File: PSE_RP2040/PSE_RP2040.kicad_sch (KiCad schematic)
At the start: 68 parts, among them IC2 SAM-M8Q-0, J1 USB_B, J2 USB_B_Mini, J3 8P8C_LED, J4 Conn_01x03, Q2 IRLML6402, SW1 SW_Push, SW2 SW_Push, U1 RP2040, U2 PCF8563T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

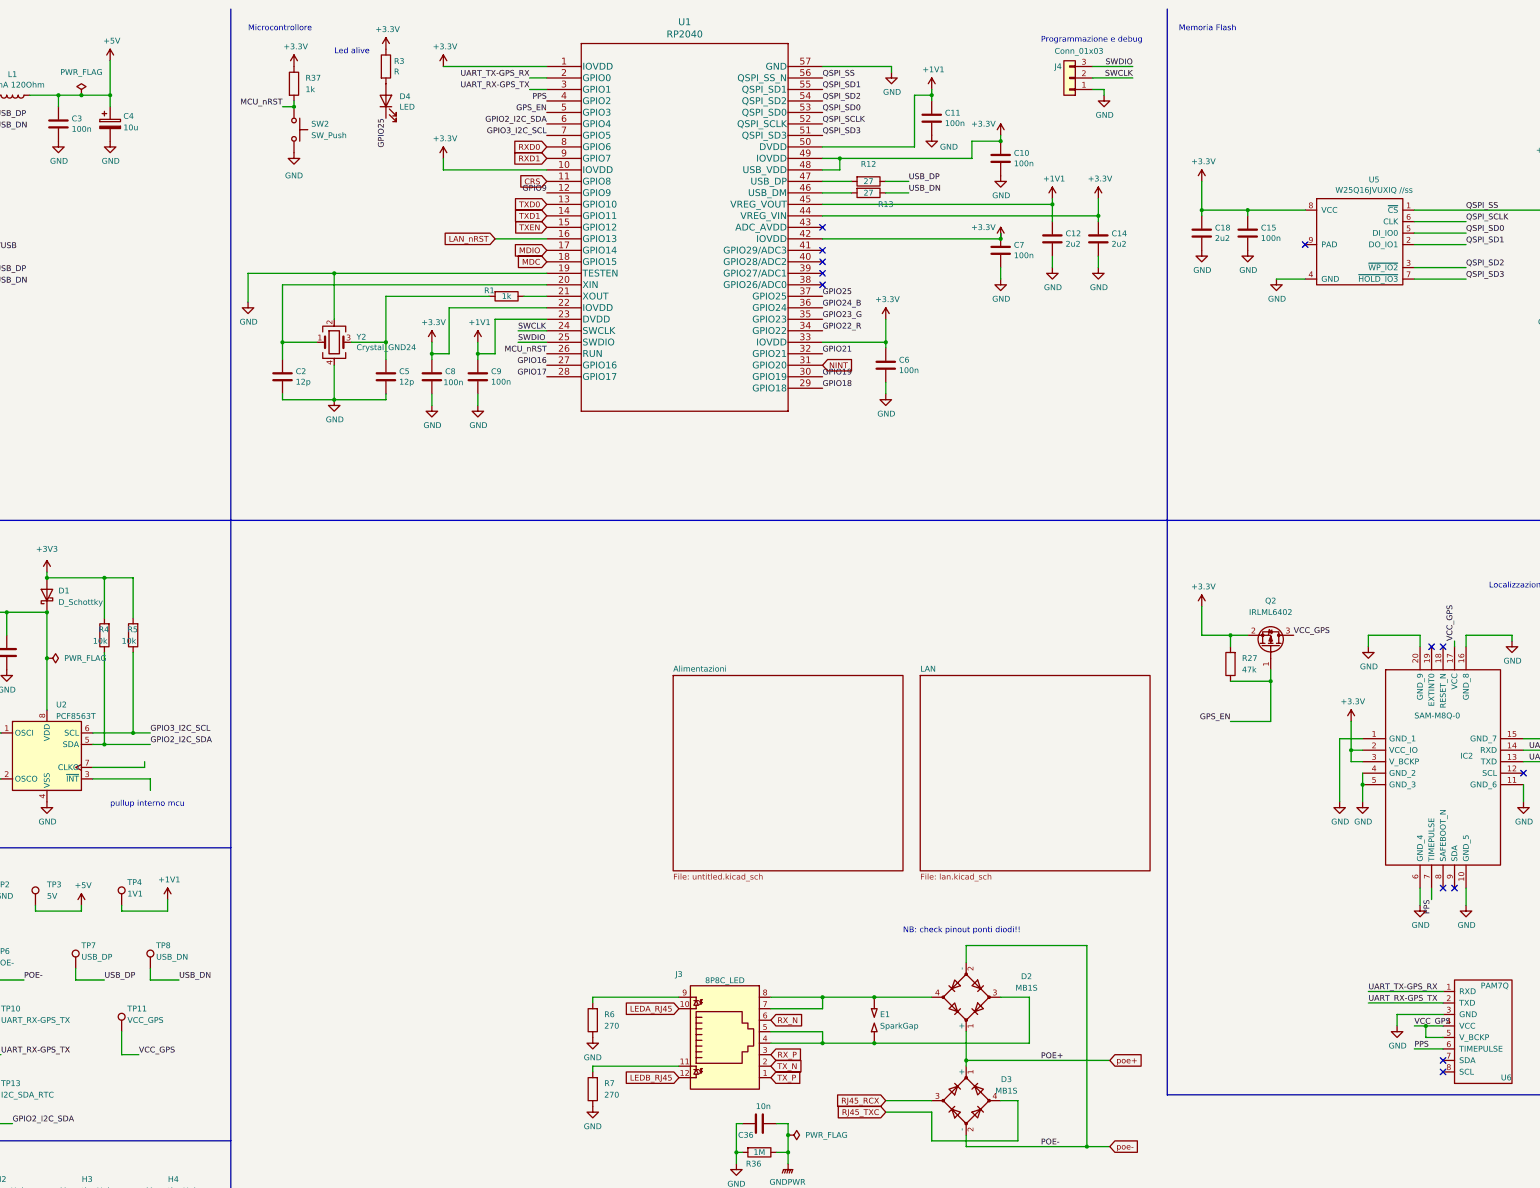
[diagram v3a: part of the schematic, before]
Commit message: check pin, footprint e symb mem
tolto pin 9 al simbolo memoria
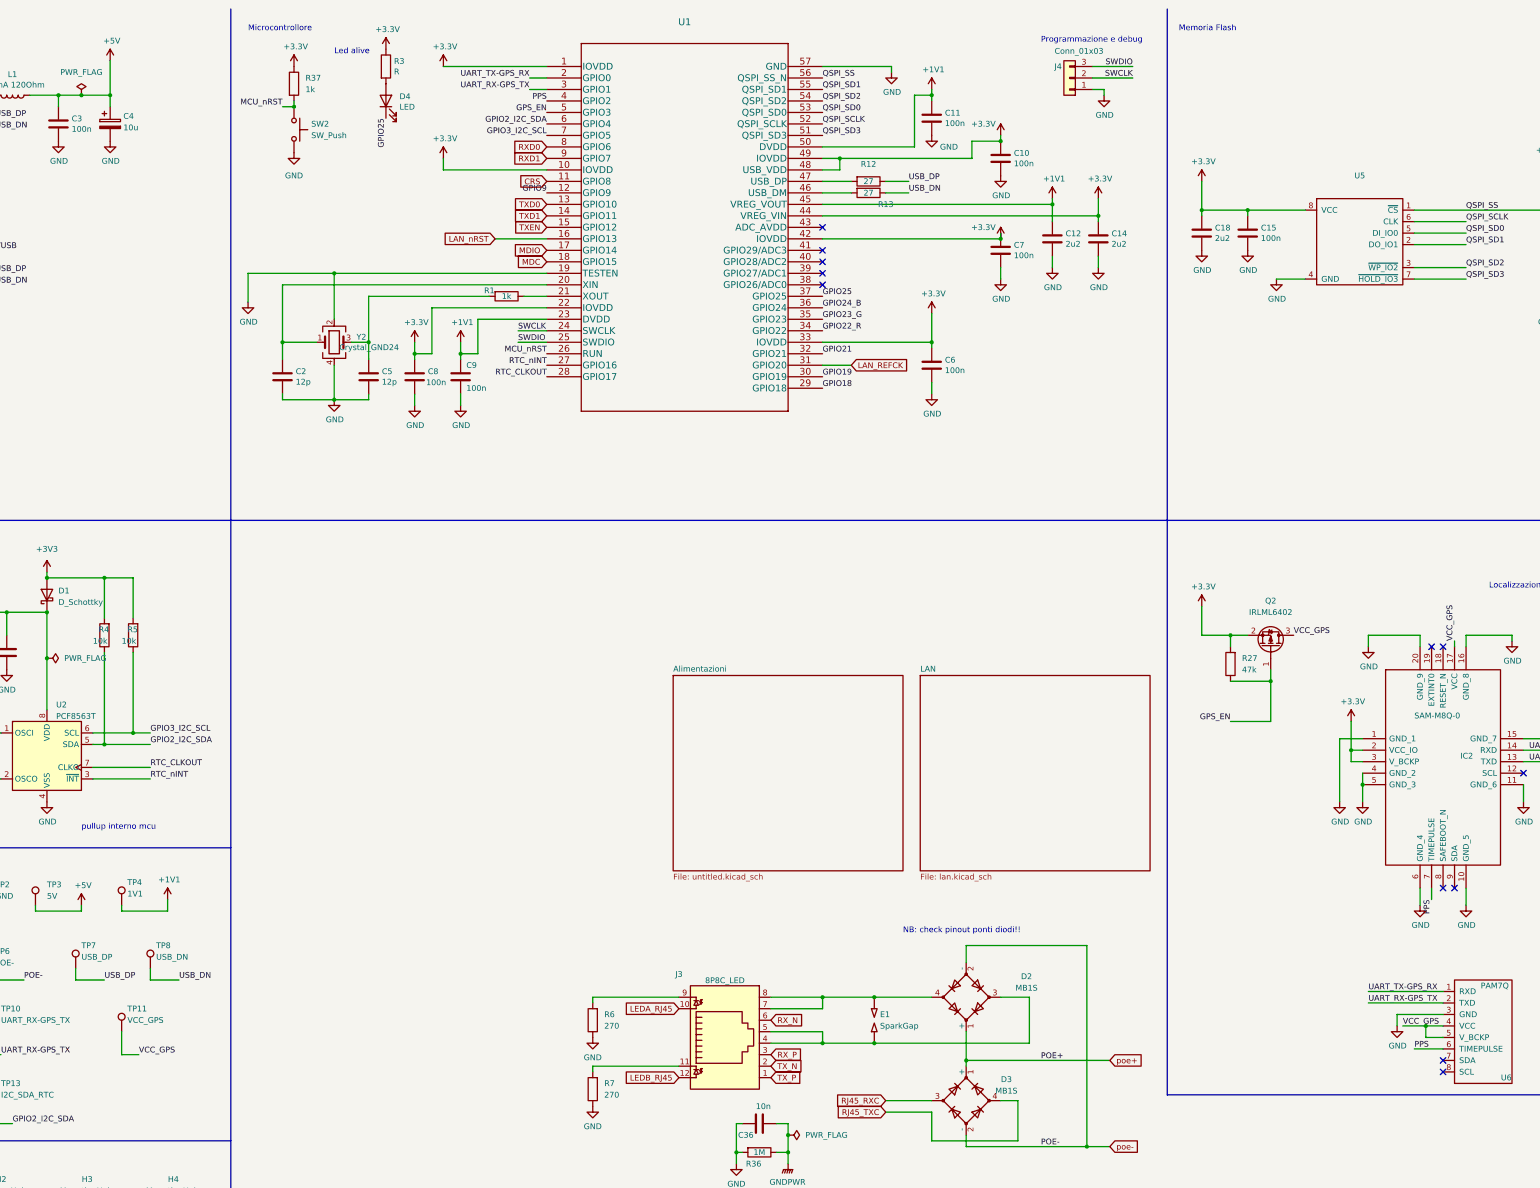
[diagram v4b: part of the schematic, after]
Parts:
- removed U5: W25Q16JVUXIQ //ss, Package_SO:SOIC-8_5.275x5.275mm_P1.27mm, symbol PSE_RP2040-rescue:W25Q16JVUXIQ-Flash_memory
- added U5: (no value), symbol pse_paganin:W25Q16JVUXIQ
- U1: value RP2040 -> (none); footprint PSE2021:RP2040-QFN-56 -> (none)
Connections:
- net GPIO16 is gone; now on net RTC_nINT: U1.27 (GPIO16)
- net GPIO17 is gone; now on net RTC_CLKOUT: U1.28 (GPIO17)
- net +3V3: now also U5.8 (VCC)
- net GND: now also U5.4 (GND)
- net QSPI_SCLK: now also U5.6 (CLK)
- net QSPI_SD0: now also U5.5 (DI_IO0)
- net QSPI_SD1: now also U5.2 (DO_IO1)
- net QSPI_SD2: now also U5.3 (~{WP_IO2})
- net QSPI_SD3: now also U5.7 (~{HOLD_IO3})
- net QSPI_SS: now also U5.1 (~{CS})
- net RTC_nINT: now reaches U2.3 (~{INT})
- net RTC_CLKOUT: now reaches U2.7 (CLKO)
- net NINT renamed LAN_REFCK
- net RJ45_RCX renamed RJ45_RXC
- no-connect marks 14 -> 13
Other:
- moved on the sheet: C5, C6, C8, C9

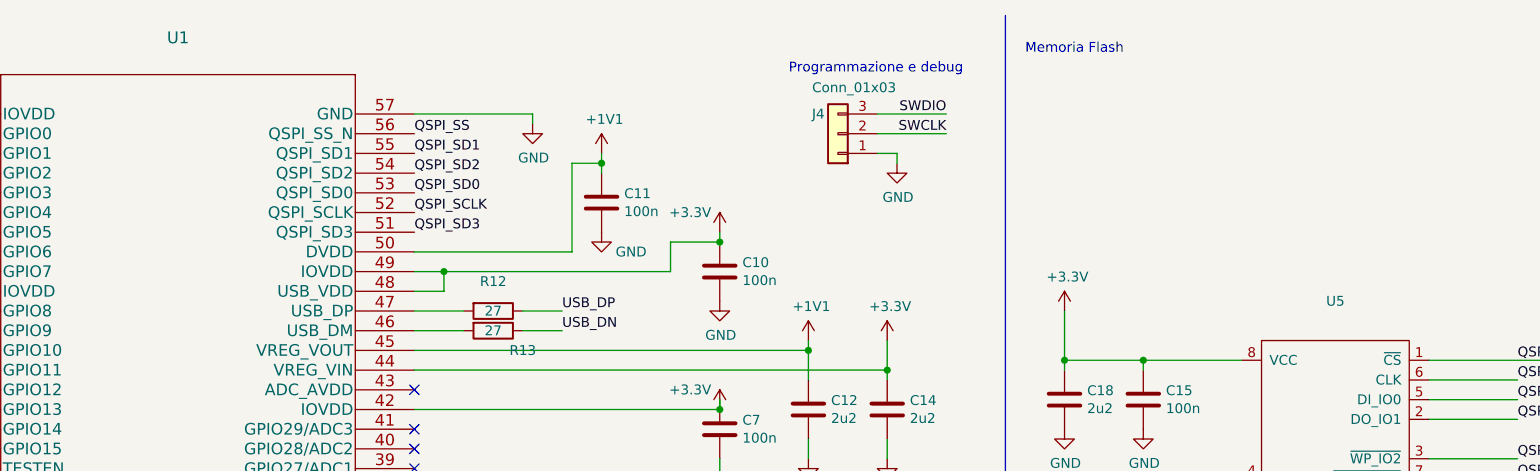
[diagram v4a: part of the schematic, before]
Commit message: piazzamento componenti pcb 1
piazzamento di massima
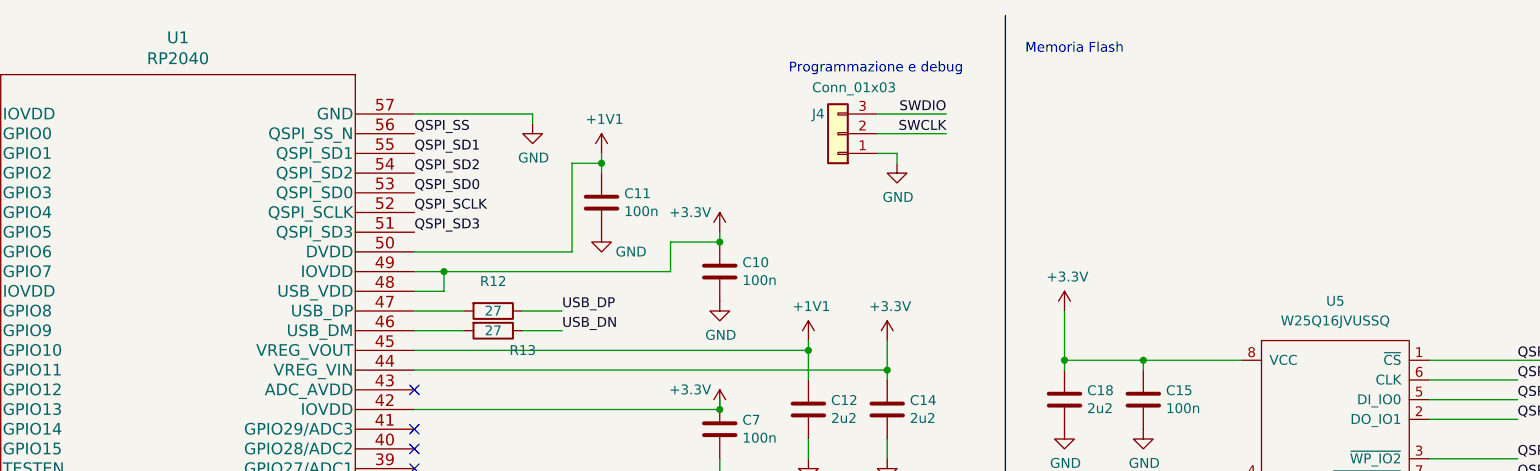
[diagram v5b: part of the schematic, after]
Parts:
- U1: value (none) -> RP2040; footprint (none) -> PSE2021:RP2040-QFN-56
- U5: value (none) -> W25Q16JVUSSQ; footprint (none) -> Package_SO:SOIC-8_5.275x5.275mm_P1.27mm
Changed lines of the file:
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@@
       (effects (font (size 1.524 1.524)))
     )
-    (property "Value" "" (id 1) (at 193.04 18.2626 0)
+    (property "Value" "RP2040" (id 1) (at 193.04 18.2626 0)
       (effects (font (size 1.524 1.524)))
     )
-    (property "Footprint" "" (id 2) (at 193.04 19.304 0)
+    (property "Footprint" "PSE2021:RP2040-QFN-56" (id 2) (at 193.04 19.304 0)
       (effects (font (size 1.524 1.524)) hide)
     )
@@
     (in_bom yes) (on_board yes) (fields_autoplaced)
     (property "Reference" "U5" (id 0) (at 342.265 49.53 0))
-    (property "Value" "" (id 1) (at 342.265 52.07 0))
-    (property "Footprint" "" (id 2) (at 341.63 63.5 0)
-      (effects (font (size 1.27 1.27)) hide)
-    )
+    (property "Value" "W25Q16JVUSSQ" (id 1) (at 342.265 52.07 0))
+    (property "Footprint" "Package_SO:SOIC-8_5.275x5.275mm_P1.27mm" (id 2) (at 341.63 63.5 0)
+      (effects (font (size 1.27 1.27)) hide)
+    )

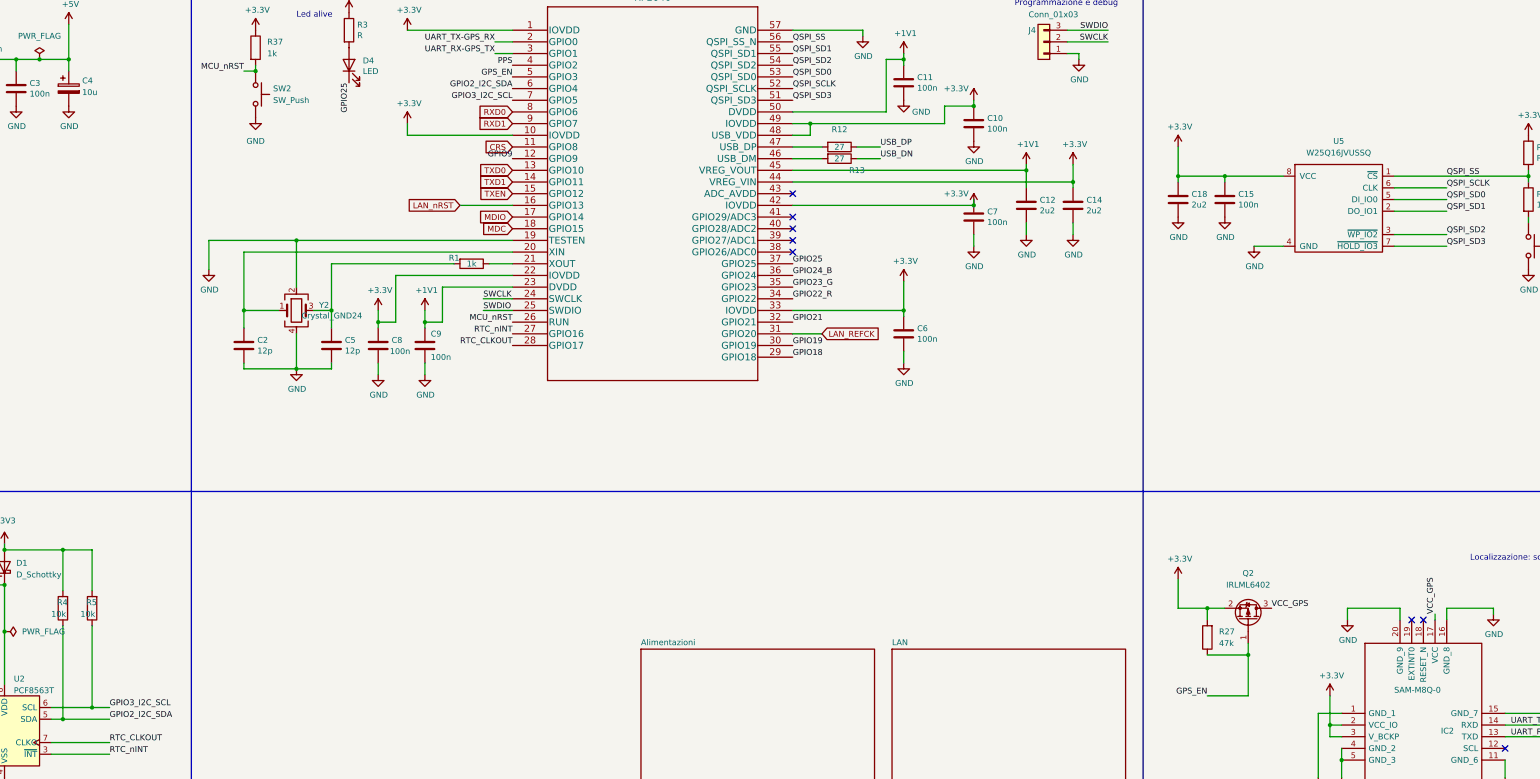
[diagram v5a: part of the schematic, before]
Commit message: pad micro, footprint, posizionamento componenti pcb
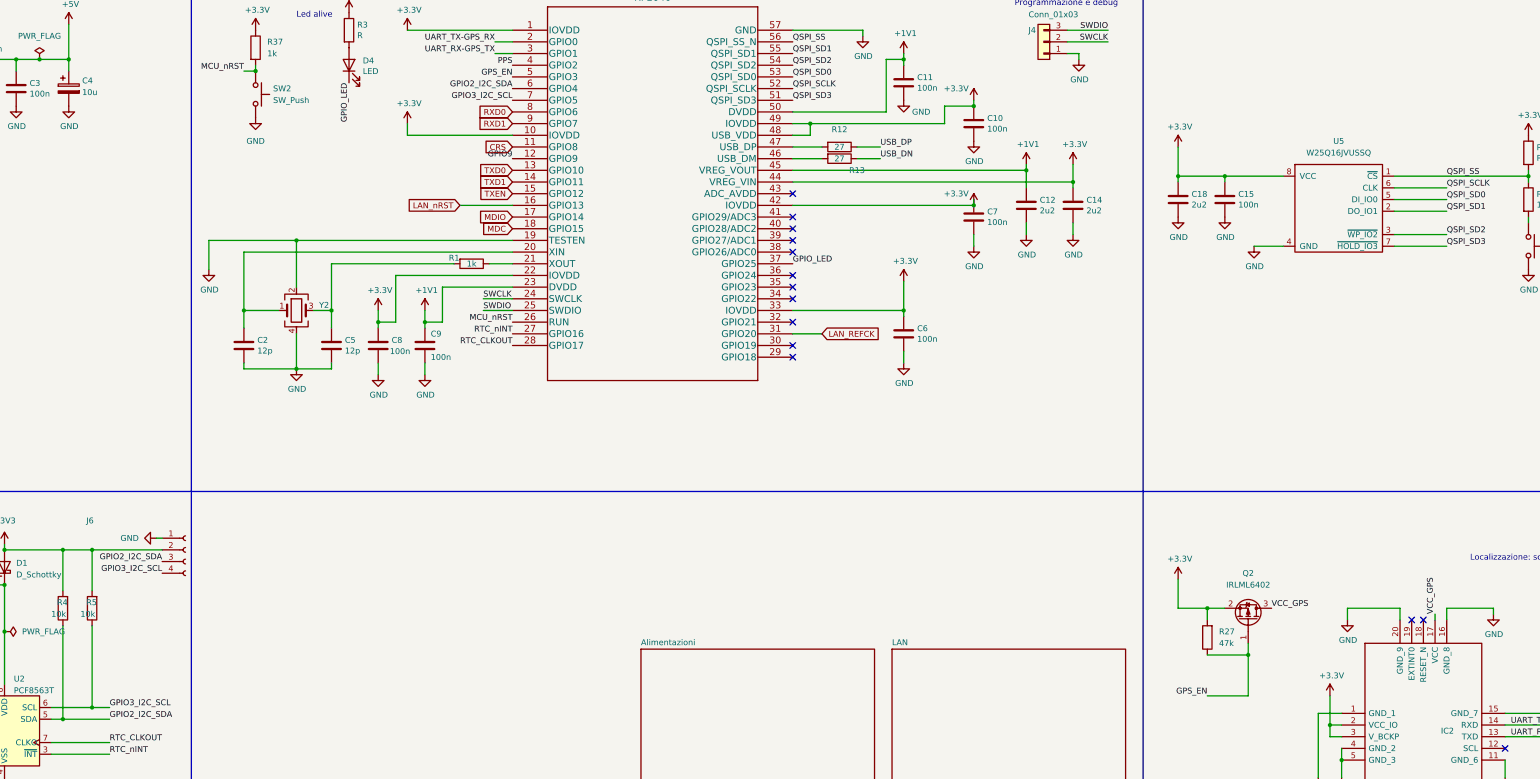
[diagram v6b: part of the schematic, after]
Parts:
- added J6: (no value), symbol Connector:Conn_01x04_Female
- IC2: value SAM-M8Q-0 -> (none); footprint PSE2021:SAM-M8Q -> (none)
- SW1, SW2: footprint Button_Switch_SMD:SW_SPST_EVQP0 -> (none)
- TP1, TP10, TP11, TP12, TP13, TP2, TP3, TP4, TP5, TP6, TP7, TP8, TP9: footprint TestPoint:TestPoint_Keystone_5005-5009_Compact -> (none)
- Y2: value Crystal_GND24 -> (none); footprint Crystal:Crystal_SMD_3225-4Pin_3.2x2.5mm_HandSoldering -> (none)
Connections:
- net +3V3: now also J6.2 (Pin_2)
- net GND: now also J6.1 (Pin_1)
- net GPIO2_I2C_SDA: now also J6.3 (Pin_3)
- net GPIO3_I2C_SCL: now also J6.4 (Pin_4)
- net GPIO18: no longer names the net of U1.29 (GPIO18)
- net GPIO19: no longer names the net of U1.30 (GPIO19)
- net GPIO21: no longer names the net of U1.32 (GPIO21)
- net GPIO22_R: no longer names the net of U1.34 (GPIO22)
- net GPIO23_G: no longer names the net of U1.35 (GPIO23)
- net GPIO24_B: no longer names the net of U1.36 (GPIO24)
- net GPIO25 renamed GPIO_LED
- no-connect marks 13 -> 19
